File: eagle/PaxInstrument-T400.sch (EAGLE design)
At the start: 122 parts, among them IC1 MCP3424, U1 MCP9800, U3 MCP73831, U4 MIC5219-3.3V, U7 USD-SOCKETNEW, U8 NC7S32, X1 FH12-12S-0.5SH, Y1 RESONATORSMD

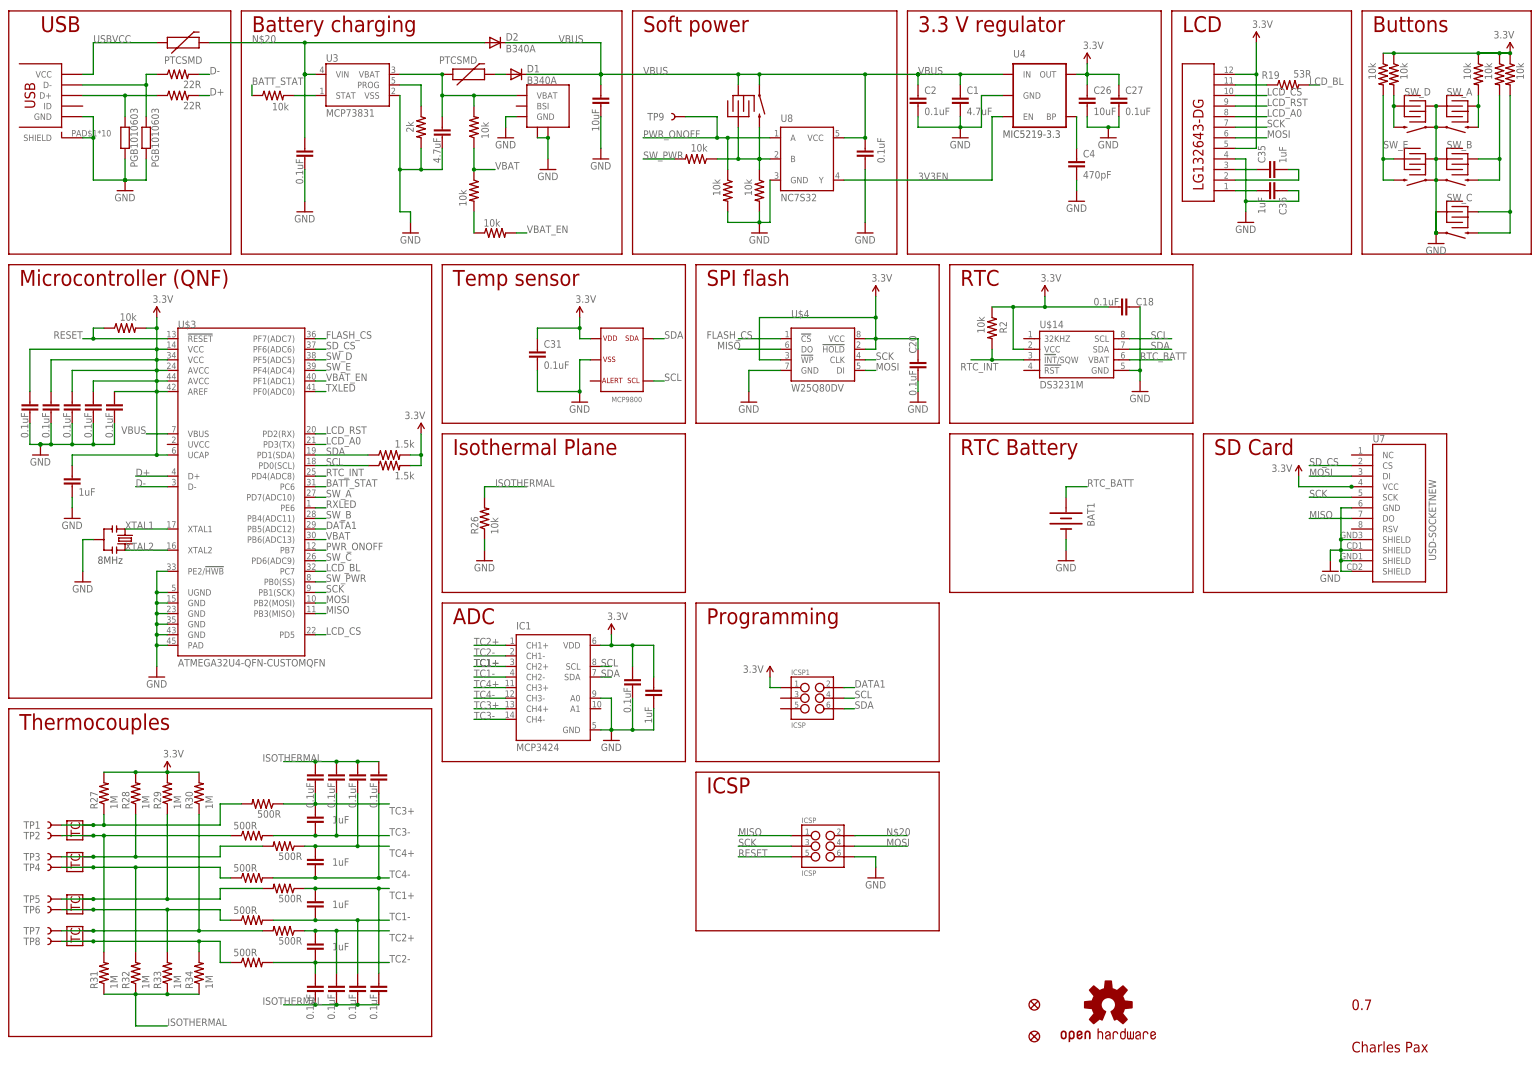
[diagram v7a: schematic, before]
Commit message: - Moved buttons 0.04 inches closer to the edge. This is to better fit the enclosure. - Renamed ICSP power in to VBUS_IN - Added labels to the SMT headers - Updated pin assignments on silkscreen
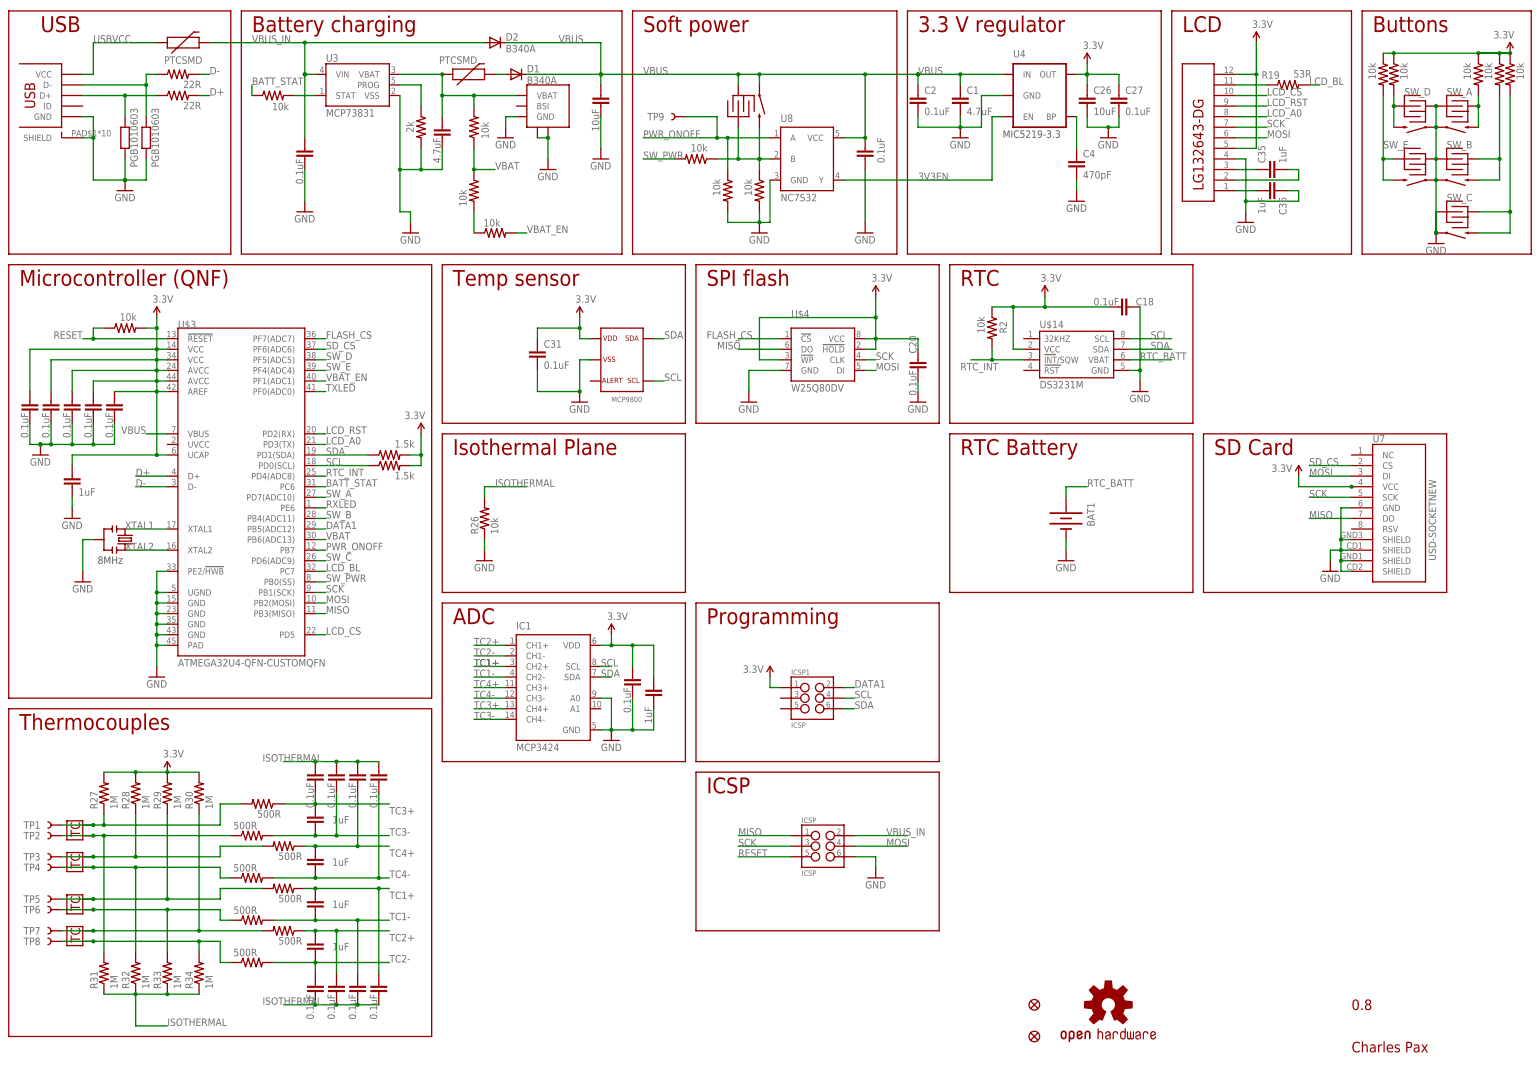
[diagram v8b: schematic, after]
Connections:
- net N$20 renamed VBUS_IN
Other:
- note added: "0.8"
- note removed: "0.7"
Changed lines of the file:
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@@
 <?xml version="1.0" encoding="utf-8"?>
 <!DOCTYPE eagle SYSTEM "eagle.dtd">
-<eagle version="7.1.0">
+<eagle version="6.5.0">
 <drawing>
 <settings>
@@
 <wire x1="111.76" y1="154.94" x2="111.76" y2="193.04" width="0.2032" layer="94"/>
 <text x="114.3" y="187.96" size="3.81" layer="94">Temp sensor</text>
-<text x="330.2" y="15.24" size="2.54" layer="94" align="center-left">0.7</text>
+<text x="330.2" y="15.24" size="2.54" layer="94" align="center-left">0.8</text>
 <wire x1="172.72" y1="73.66" x2="231.14" y2="73.66" width="0.2032" layer="94"/>
 <wire x1="172.72" y1="111.76" x2="172.72" y2="73.66" width="0.2032" layer="94"/>
@@
 </segment>
 </net>
-<net name="N$20" class="0">
+<net name="VBUS_IN" class="0">
 <segment>
 <pinref part="U3" gate="G$1" pin="VIN"/>
